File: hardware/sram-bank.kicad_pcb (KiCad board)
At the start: 2 copper layers, 50.8 x 78.7 mm, 38 parts, among them U1 74AHC1G00GV,125, U10 SN74LVC8T245DWRG4, U11 SN74LVC8T245DWRG4, U12 IS66WV51216EBLL-55TLI, U2 SN74LVC8T245DWRG4, U3 SN74LVC8T245DWRG4, U4 SN74LVC8T245DWRG4, U5 SN74LVC8T245DWRG4, U6 SN74LVC8T245DWRG4, U7 SN74LVC8T245DWRG4, U8 SN74LVC8T245DWRG4, U9 SN74LVC8T245DWRG4

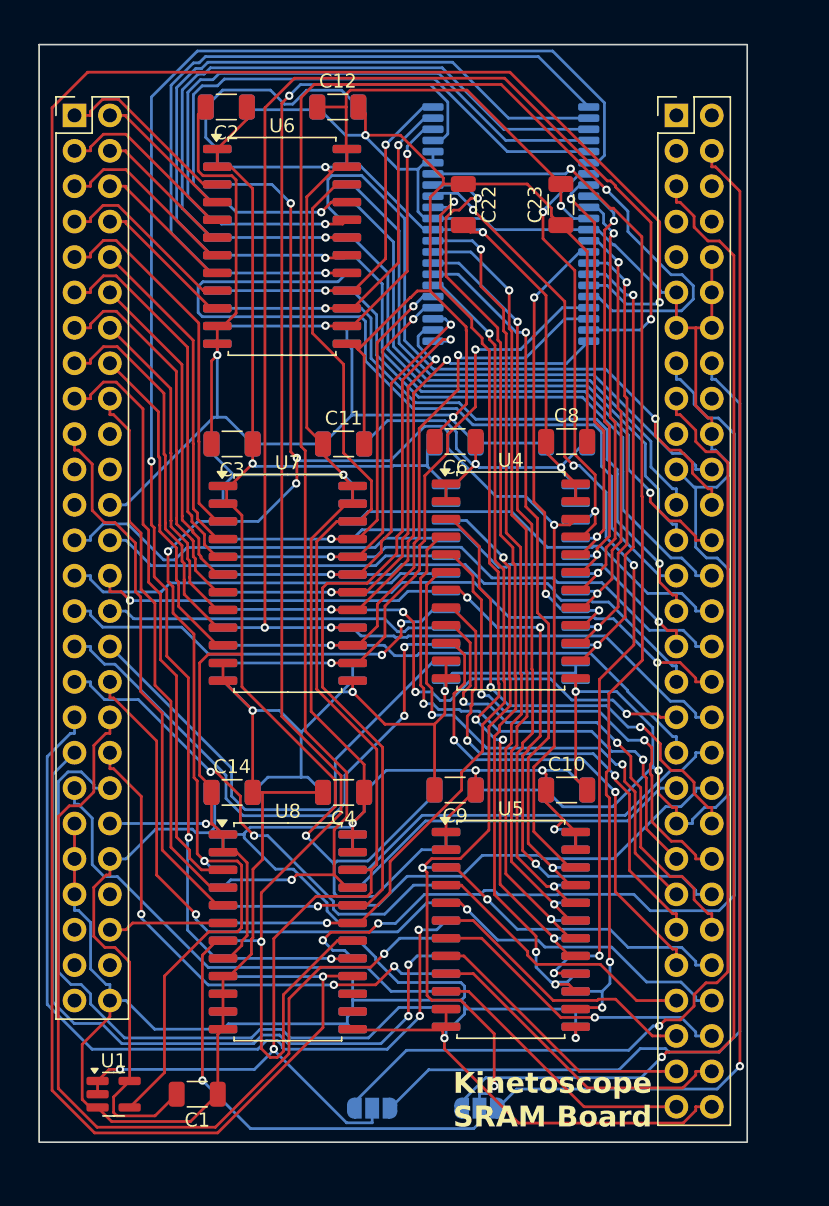
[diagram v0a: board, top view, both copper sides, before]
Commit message: Massively reorganize board designs
Now planning to have most assembly done by JLCPCB, so trace sizes,
part selections, etc. are set accordingly.

New boards are:
 - cartridge interface & flash
 - microcontroller & registers
 - sram x2
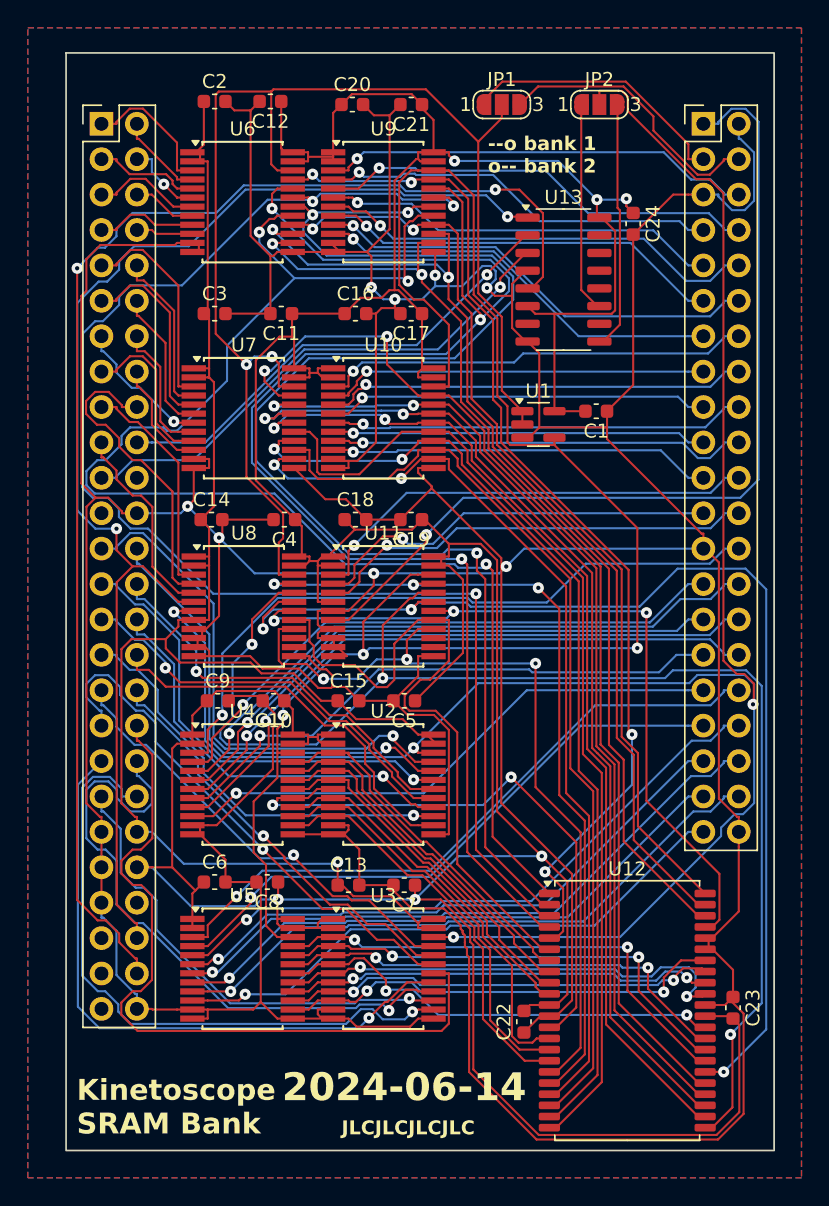
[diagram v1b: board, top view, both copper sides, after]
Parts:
- added C24: 22nF, Capacitor_SMD:C_0603_1608Metric, F.Cu at (59.4, 31.6)
- added J2: ~, Connector_PinHeader_2.54mm:PinHeader_2x21_P2.54mm_Vertical, F.Cu at (64.5, 24.4)
- added U13: decoder, Package_SO:SO-16_3.9x9.9mm_P1.27mm, F.Cu at (54.4, 35.6)
- added X1: ~, kinetoscope-cart-header:kinetoscope-cart-board-template, F.Cu at (21.3, 24.4)
- C1, C10, C11, C12, C14, C2, C22, C23, C3, C4, C6, C8, C9: footprint Capacitor_SMD:C_1206_3216Metric -> Capacitor_SMD:C_0603_1608Metric
- C13, C15, C16, C17, C18, C19, C20, C21, C5, C7: footprint Capacitor_SMD:C_1206_3216Metric -> Capacitor_SMD:C_0603_1608Metric; moved to F.Cu
- J1: footprint kinetoscope-cart-header:kinetoscope-cart-header -> Connector_PinHeader_2.54mm:PinHeader_2x26_P2.54mm_Vertical
- JP1, JP2: moved to F.Cu
- U1: value 74AHC1G00GV,125 -> NAND
- U10, U11, U2, U3, U9: value SN74LVC8T245DWRG4 -> 3.3V <=> 5V; footprint Package_SO:SOIC-24W_7.5x15.4mm_P1.27mm -> Package_SO:SSOP-24_5.3x8.2mm_P0.65mm; moved to F.Cu
- U12: value IS66WV51216EBLL-55TLI -> PSRAM; moved to F.Cu
- U4, U5, U6, U7, U8: value SN74LVC8T245DWRG4 -> 3.3V <=> 5V; footprint Package_SO:SOIC-24W_7.5x15.4mm_P1.27mm -> Package_SO:SSOP-24_5.3x8.2mm_P0.65mm
- moved JP1 72.6 mm to (50.0, 23.0), turned to 0 degrees
- moved JP2 72.5 mm to (57.0, 23.0), turned to 0 degrees
- moved C23 58.9 mm to (66.6, 87.8), turned to -90 degrees
- moved C22 58.8 mm to (51.6, 88.8), turned to 90 degrees
- moved U12 57.0 mm to (59.0, 88.0), turned to 0 degrees
- moved U1 56.9 mm to (52.6, 46.0)
- moved C1 56.7 mm to (56.8, 45.0)
- moved C8 38.2 mm to (33.2, 78.8), turned to 180 degrees
- moved C6 36.0 mm to (29.4, 78.8), turned to 0 degrees
- moved U11 24.3 mm to (41.5, 59.0), turned to 0 degrees
- moved U4 24.2 mm to (31.4, 71.8)
- moved U8 23.6 mm to (31.5, 59.0)
- moved C10 22.0 mm to (33.6, 65.8), turned to 180 degrees
- moved C5 21.9 mm to (43.0, 65.8)
- moved C18 21.5 mm to (39.5, 52.8)
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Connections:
- net /3V renamed +3.3V
- net /5V renamed +5V
- net /~{ESP32_CONTROL} renamed /~{UC_CONTROL}
- C1 pad 1: /GND -> GND
- C10 pad 2: /GND -> GND
- C11 pad 2: /GND -> GND
- C12 pad 2: /GND -> GND
- C13 pad 2: /GND -> GND
- C14 pad 2: /GND -> GND
- C15 pad 2: /GND -> GND
- C16 pad 2: /GND -> GND
- C17 pad 2: /GND -> GND
- C18 pad 2: /GND -> GND
- C19 pad 2: /GND -> GND
- C2 pad 2: /GND -> GND
- C20 pad 2: /GND -> GND
- C21 pad 2: /GND -> GND
- C22 pad 1: /GND -> GND
- C23 pad 1: /GND -> GND
- C3 pad 2: /GND -> GND
- C4 pad 2: /GND -> GND
- C5 pad 2: /GND -> GND
- C6 pad 2: /GND -> GND
- C7 pad 2: /GND -> GND
- C8 pad 2: /GND -> GND
- C9 pad 2: /GND -> GND
- J1 pad 20: /kinetoscope-header-internal/SEGA_A20 -> /SEGA_A20
- J1 pad 21: /kinetoscope-header-internal/SEGA_A21 -> /SEGA_A21
- J1 pad 24: /GND -> GND
- J1 pad 41: /GND -> GND
- J1 pad 43: /GND -> GND
- J1 pad 45: /GND -> GND
- J1 pad 50: /kinetoscope-header-internal/~{SEGA_AS} -> /~{SEGA_AS}
- J1 pad 52: /GND -> GND
- U1 pad 3: /GND -> GND
- U10 pad 11: /GND -> GND
- U10 pad 12: /GND -> GND
- U10 pad 13: /GND -> GND
- U11 pad 10: /GND -> GND
- U11 pad 11: /GND -> GND
- U11 pad 12: /GND -> GND
- U11 pad 13: /GND -> GND
- U11 pad 7: /GND -> GND
- U11 pad 9: /GND -> GND
- U12 pad 12: /GND -> GND
- U12 pad 34: /GND -> GND
- U12 pad 39: /GND -> GND
- U12 pad 40: /GND -> GND
- U2 pad 11: /GND -> GND
- U2 pad 12: /GND -> GND
- U2 pad 13: /GND -> GND
- U3 pad 11: /GND -> GND
- U3 pad 12: /GND -> GND
- U3 pad 13: /GND -> GND
- U4 pad 11: /GND -> GND
- U4 pad 12: /GND -> GND
- U4 pad 13: /GND -> GND
- U5 pad 11: /GND -> GND
- U5 pad 12: /GND -> GND
- U5 pad 13: /GND -> GND
- U6 pad 11: /GND -> GND
- U6 pad 12: /GND -> GND
- U6 pad 13: /GND -> GND
- U7 pad 11: /GND -> GND
- U7 pad 12: /GND -> GND
- U7 pad 13: /GND -> GND
- U8 pad 10: /GND -> GND
- U8 pad 11: /GND -> GND
- U8 pad 12: /GND -> GND
- U8 pad 13: /GND -> GND
- U8 pad 9: /GND -> GND
- U9 pad 11: /GND -> GND
- U9 pad 12: /GND -> GND
- U9 pad 13: /GND -> GND
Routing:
- net GND: track 0.00 -> 545.6 mm, vias 0 -> 8
- net /GND: track 491.9 -> 0.00 mm, vias 10 -> 0
- net /~{SRAM_FINAL_WE}: track 167.9 -> 58.5 mm, vias 2 -> 3
- net /~{SEGA_AS}: track 0.00 -> 95.9 mm, vias 0 -> 2
- net /~{SEGA_CE}: track 8.32 -> 91.5 mm, vias 0 -> 2
- net /~{SRAM_CE1}: track 85.3 -> 15.1 mm, vias 1 -> 0
- net /~{SRAM_CE2}: track 85.3 -> 17.8 mm, vias 1 -> 0
- net /~{SRAM_FINAL_CE}: track 114.2 -> 49.0 mm, vias 3 -> 0
- net /SRAM_DIS_1: track 76.5 -> 19.6 mm
- net /SRAM_A1: track 51.1 -> 107.2 mm, vias 1 -> 3
- net /~{SRAM_CE}: track 88.2 -> 143.2 mm
- net /SRAM_DIS_2: track 74.8 -> 20.0 mm, vias 1 -> 0
- net /SRAM_A16: track 112.1 -> 60.2 mm, vias 2 -> 3
- net /SRAM_A2: track 52.8 -> 103.3 mm, vias 1 -> 3
- net /~{SRAM_FINAL_OE}: track 103.9 -> 55.9 mm, vias 2 -> 3
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- added copper zone on B.Cu, net GND
- added copper zone on F.Cu, net GND
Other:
- board text added: "--o bank 1 o-- bank 2"
- board text added: "2024-06-14"
- board text added: "JLCJLCJLCJLC"
- board text added: "Kinetoscope SRAM Bank"
- board text removed: "Kinetoscope SRAM Board"

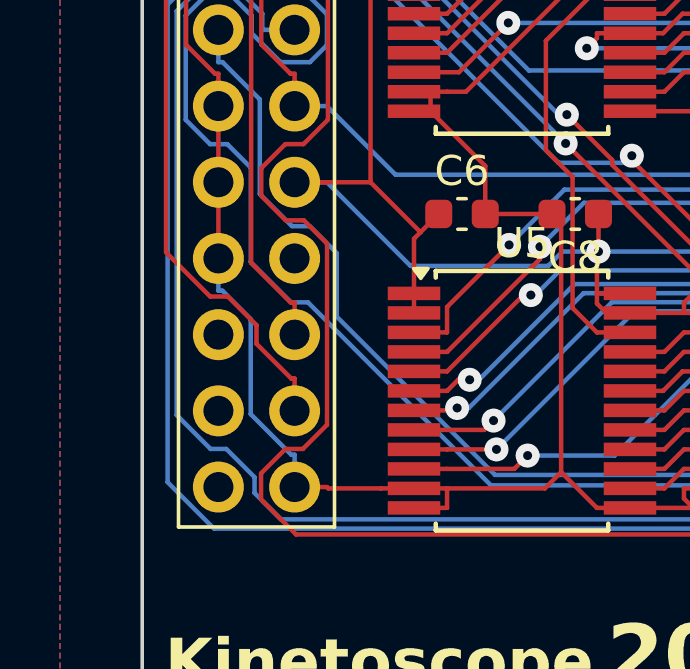
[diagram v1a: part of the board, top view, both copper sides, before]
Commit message: Update interboard header in microcontroller and SRAM boards
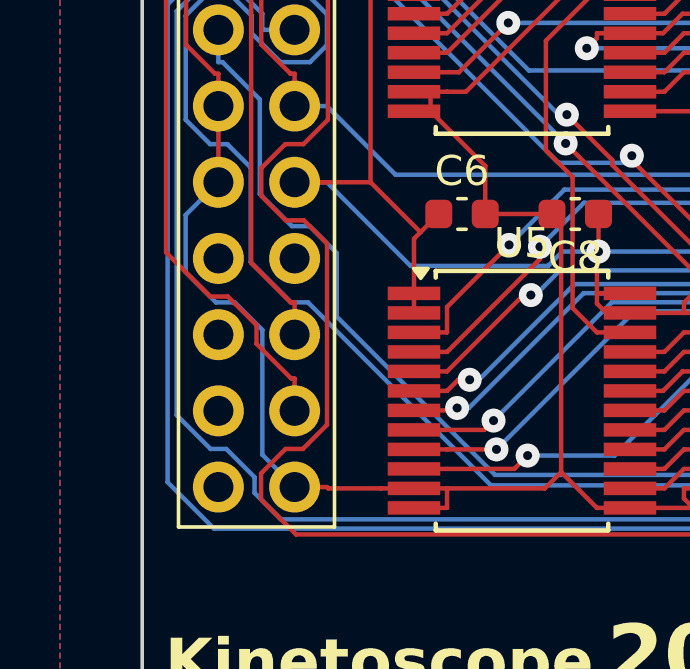
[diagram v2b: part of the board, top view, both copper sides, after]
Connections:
- J1 pad 45: GND -> /kinetoscope-header-internal/~{SEGA_OE}
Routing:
- net GND: track 545.6 -> 546.8 mm
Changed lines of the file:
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@@
 	(net 138 "GND")
 	(net 139 "+5V")
+	(net 140 "/kinetoscope-header-internal/~{SEGA_OE}")
 	(footprint "Package_SO:SSOP-24_5.3x8.2mm_P0.65mm"
 		(layer "F.Cu")
@@
 			(layers "*.Cu" "*.Mask")
 			(remove_unused_layers no)
-			(net 138 "GND")
-			(pinfunction "GND")
-			(pintype "passive")
+			(net 140 "/kinetoscope-header-internal/~{SEGA_OE}")
+			(pinfunction "~{SEGA_OE}")
+			(pintype "passive+no_connect")
 		)
 		(pad "46" thru_hole oval
@@
 	)
 	(segment
-		(start 21.28 77.72)
-		(end 21.28 80.26)
-		(width 0.15)
-		(layer "F.Cu")
-		(net 138)
-	)
-	(segment
 		(start 49.9627 56.1409)
 		(end 49.9627 55.5313)
@@
 	)
 	(segment
-		(start 22.3567 85.4516)
-		(end 23.7084 86.8033)
-		(width 0.15)
-		(layer "B.Cu")
-		(net 138)
-	)
-	(segment
-		(start 21.28 80.26)
-		(end 21.28 81.3367)
-		(width 0.15)
-		(layer "B.Cu")
-		(net 138)
-	)
-	(segment
 		(start 48.6122 34.5825)
 		(end 49.1961 34.5825)
@@
 	)
 	(segment
-		(start 23.82 87.88)
-		(end 23.82 86.8033)
-		(width 0.15)
-		(layer "B.Cu")
-		(net 138)
-	)
-	(segment
-		(start 22.3567 82.2787)
-		(end 22.3567 85.4516)
+		(start 22.745 82.645)
+		(end 22.745 86.805)
 		(width 0.15)
 		(layer "B.Cu")
@@
 	)
 	(segment
-		(start 21.4147 81.3367)
-		(end 22.3567 82.2787)
-		(width 0.15)
-		(layer "B.Cu")
-		(net 138)
-	)
-	(segment
 		(start 67 25.4567)
 		(end 67.1115 25.4567)
@@
 	)
 	(segment
+		(start 21.825 81.725)
+		(end 22.745 82.645)
+		(width 0.15)
+		(layer "B.Cu")
+		(net 138)
+	)
+	(segment
 		(start 68.0971 26.4423)
 		(end 68.0971 29.901)
@@
 	)
 	(segment
-		(start 21.28 81.3367)
-		(end 21.4147 81.3367)
+		(start 21.28 77.72)
+		(end 20.1891 78.8109)
+		(width 0.15)
+		(layer "B.Cu")
+		(net 138)
+	)
+	(segment
+		(start 20.1891 80.7141)
+		(end 21.2 81.725)
 		(width 0.15)
 		(layer "B.Cu")
@@
 	)
 	(segment
+		(start 20.1891 78.8109)
+		(end 20.1891 80.7141)
+		(width 0.15)
+		(layer "B.Cu")
+		(net 138)
+	)
+	(segment
 		(start 49.5632 35.5343)
 		(end 48.9365 36.161)
@@
 	)
 	(segment
-		(start 26.9657 52.32)
-		(end 27.4621 51.8236)
+		(start 21.2 81.725)
+		(end 21.825 81.725)
 		(width 0.15)
 		(layer "B.Cu")
@@
 	)
 	(segment
-		(start 23.7084 86.8033)
-		(end 23.82 86.8033)
+		(start 26.9657 52.32)
+		(end 27.4621 51.8236)
 		(width 0.15)
 		(layer "B.Cu")
@@
 		(width 0.15)
 		(layer "B.Cu")
+		(net 138)
+	)
+	(segment
+		(start 22.745 86.805)
+		(end 23.82 87.88)
+		(width 0.15)
+		(layer "B.Cu")

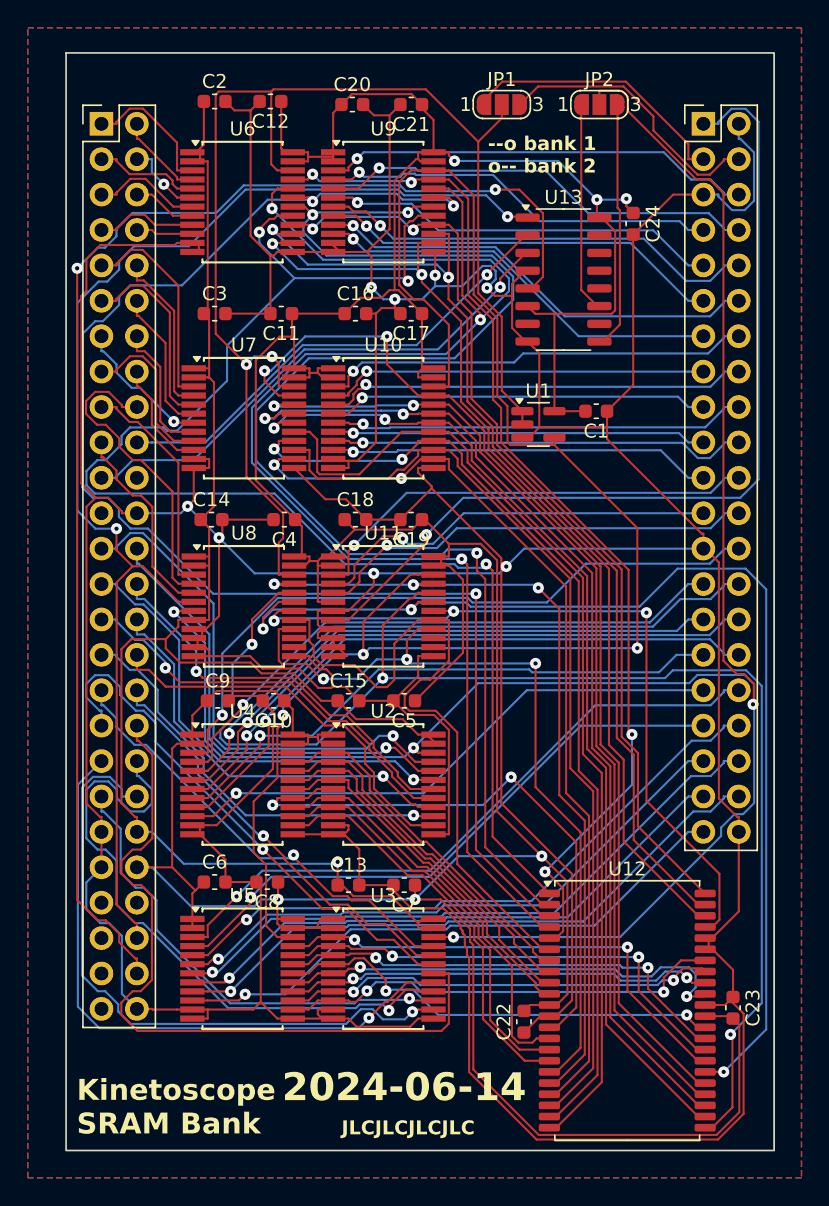
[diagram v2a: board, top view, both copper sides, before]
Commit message: Redesign SRAM address decoders
 - Redo original address decoder for SRAM_CE signal
 - Replace NAND gate with another address decoder
   - Simplifies the BOM by removing a one-off part
   - Stabilizes the control signals by making sure SEGA_CONTROL and
     UC_CONTROL can never be active at once (one does not depend on
     the other)
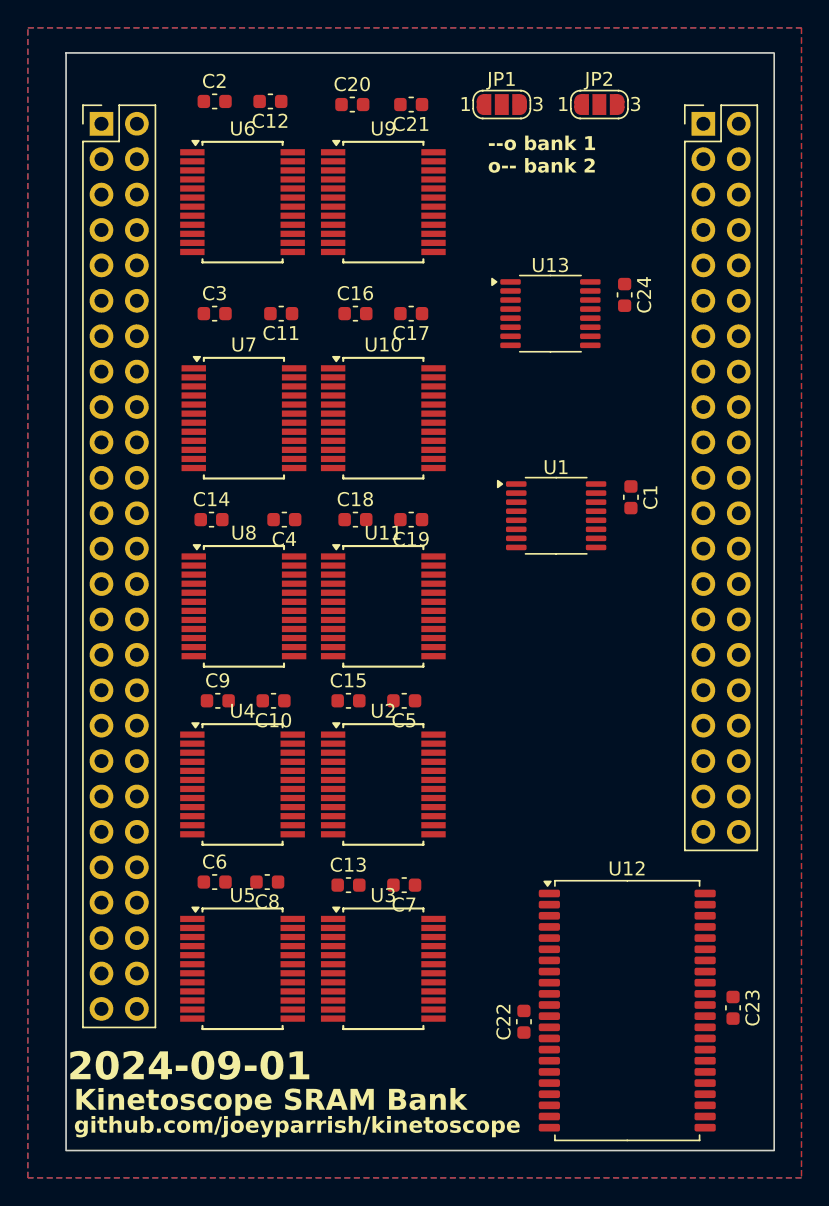
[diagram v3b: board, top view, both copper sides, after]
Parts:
- U1: value NAND -> 74LVC138A; footprint Package_TO_SOT_SMD:SC-74A-5_1.55x2.9mm_P0.95mm -> Package_SO:TSSOP-16_4.4x5mm_P0.65mm
- U10, U11, U2, U3, U4, U5, U6, U7, U8, U9: value 3.3V <=> 5V -> 74LVC8T245
- U12: value PSRAM -> IS66WV51216EALL
- U13: value decoder -> 74LVC138A; footprint Package_SO:SO-16_3.9x9.9mm_P1.27mm -> Package_SO:TSSOP-16_4.4x5mm_P0.65mm
- moved U1 6.67 mm to (53.9, 52.5)
- moved C1 6.66 mm to (59.3, 51.2), turned to -90 degrees
- moved C24 5.14 mm to (58.8, 36.7)
- moved U13 2.62 mm to (53.5, 38.0)
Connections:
- C1 pad 1: GND -> +3.3V
- C1 pad 2: +3.3V -> GND
- JP1 pad 2: /~{SEGA_CONTROL} -> /SRAM_DIS
- U1 pad 1: /~{SEGA_CONTROL} -> /SRAM_DIS
- U1 pad 2: /~{SEGA_CONTROL} -> GND
- U1 pad 4: /~{UC_CONTROL} -> GND
- U1 pad 5: +3.3V -> GND
- U13 pad 1: /~{SEGA_CE} -> /SEGA_A20
- U13 pad 11: /~{SRAM_CE1} -> unconnected-(U13-~{Y4}-Pad11)
- U13 pad 2: /SEGA_A20 -> GND
- U13 pad 3: /SEGA_A21 -> GND
- U13 pad 4: GND -> /~{SEGA_CE}
- U13 pad 6: +3.3V -> /SEGA_A21
- U13 pad 7: unconnected-(U13-Y7-Pad7) -> /~{SRAM_CE1}
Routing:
- net GND: track 546.8 -> 0.00 mm, vias 8 -> 0
- net +3.3V: track 326.1 -> 0.00 mm, vias 6 -> 0
- net /~{SRAM_CE}: track 143.2 -> 0.00 mm, vias 4 -> 0
- net /~{UC_CONTROL}: track 120.0 -> 0.00 mm, vias 3 -> 0
- net +5V: track 115.6 -> 0.00 mm, vias 1 -> 0
- net /SRAM_A1: track 107.2 -> 0.00 mm, vias 3 -> 0
- net /SRAM_A2: track 103.3 -> 0.00 mm, vias 3 -> 0
- net /SRAM_A4: track 102.5 -> 0.00 mm, vias 3 -> 0
- net /SRAM_A3: track 102.0 -> 0.00 mm, vias 3 -> 0
- net /SRAM_A17: track 97.1 -> 0.00 mm, vias 3 -> 0
- net /~{SEGA_AS}: track 95.9 -> 0.00 mm, vias 2 -> 0
- net /~{SEGA_CONTROL}: track 95.6 -> 0.00 mm, vias 2 -> 0
- net /~{SEGA_CE}: track 91.5 -> 0.00 mm, vias 2 -> 0
- net /SRAM_A18: track 81.7 -> 0.00 mm, vias 3 -> 0
- net /SRAM_A8: track 77.7 -> 0.00 mm, vias 2 -> 0
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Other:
- board text added: "2024-09-01"
- board text added: "github.com/joeyparrish/kinetoscope"
- board text removed: "2024-06-14"
- board text removed: "JLCJLCJLCJLC"
